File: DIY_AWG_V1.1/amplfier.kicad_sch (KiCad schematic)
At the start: 22 parts, among them IC3 LMH6505MAX, IC4 THS3091DDAR

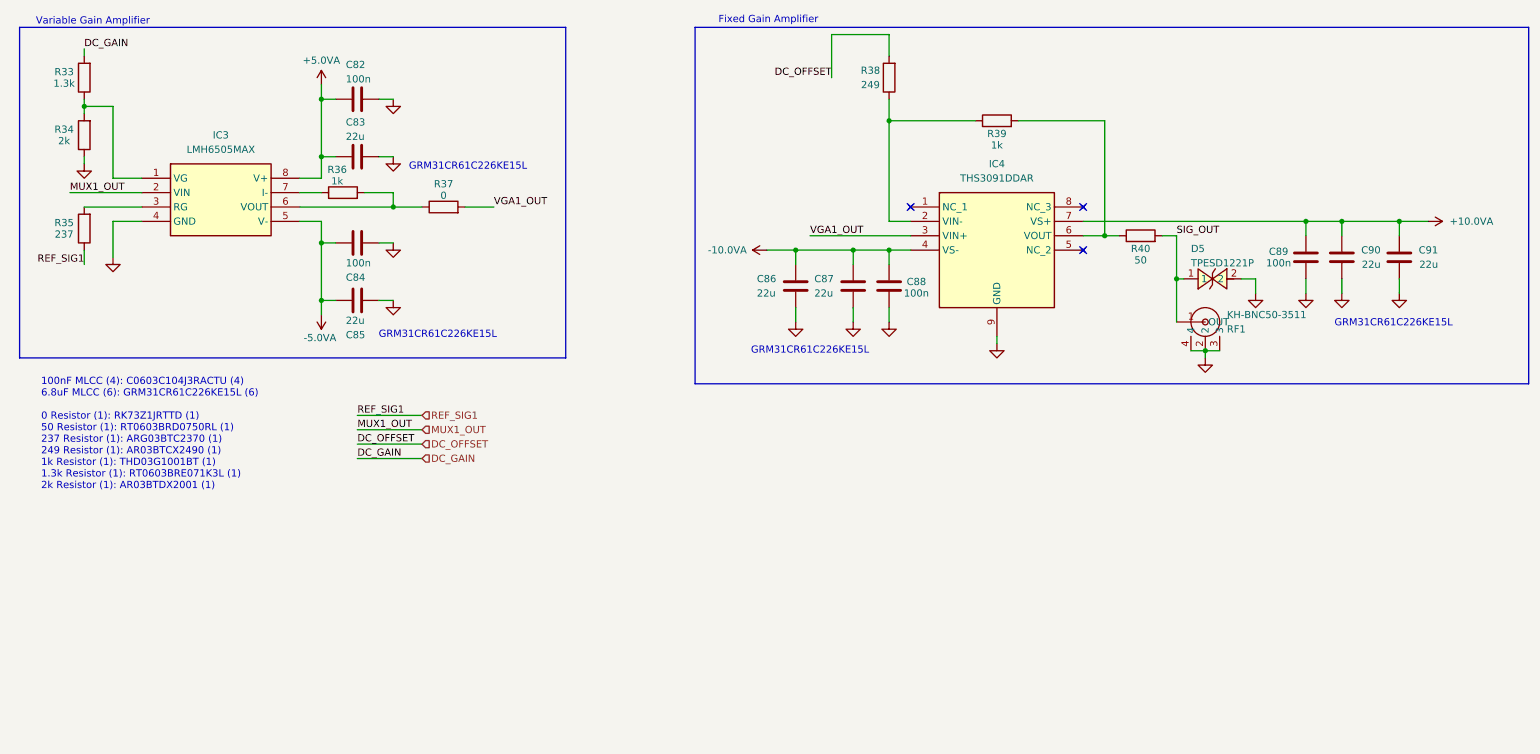
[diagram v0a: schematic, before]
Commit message: Updated to fix all ERCs
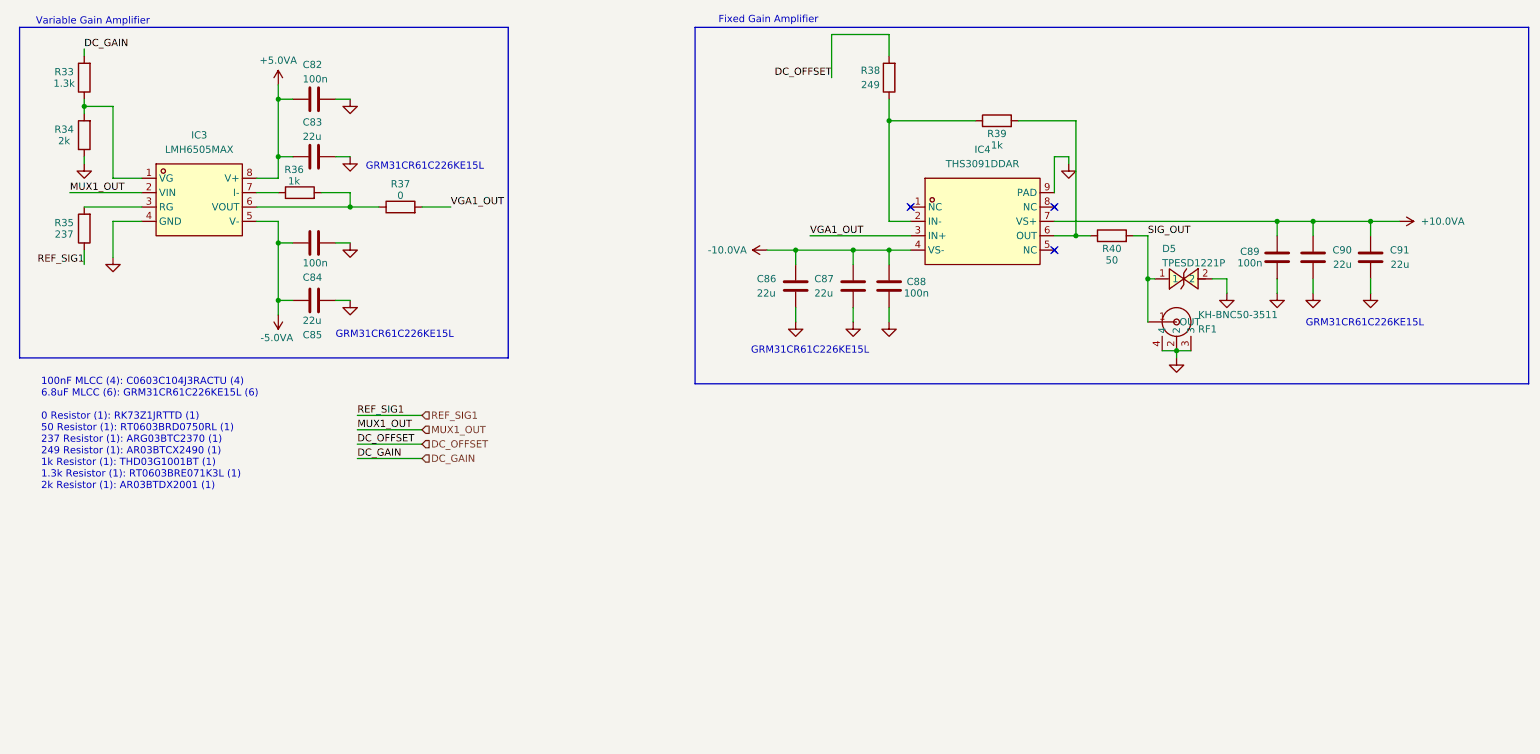
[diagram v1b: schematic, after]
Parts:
- removed IC3: LMH6505MAX, easyeda2kicad:SOP-8_L4.9-W3.9-P1.27-LS6.0-BL, symbol LMH6505MAX:LMH6505MAX
- removed IC4: THS3091DDAR, easyeda2kicad:SOIC-8_L4.9-W3.9-P1.27-LS6.0-BL-EP, symbol THS3091DDAR:THS3091DDAR
- added IC3: LMH6505MAX, easyeda2kicad:SOP-8_L4.9-W3.9-P1.27-LS6.0-BL, symbol easyeda2kicad:LMH6505MAX_NOPB
- added IC4: THS3091DDAR, easyeda2kicad:SOIC-8_L4.9-W3.9-P1.27-LS6.0-BL-EP, symbol easyeda2kicad:THS3091DDAR
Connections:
- net +10.0VA: now also IC4.7 (VS+)
- net +5.0VA: now also IC3.8 (V+)
- net -10.0VA: now also IC4.4 (VS-)
- net -5.0VA: now also IC3.5 (V-)
- net GND: now also IC3.4 (GND), IC4.9 (PAD)
- net MUX1_OUT: now also IC3.2 (VIN)
- net VGA1_OUT: now also IC4.3 (IN+)
- net at R39.2, R40.1: now also IC4.6 (OUT)
- net at R33.1, R34.2: now also IC3.1 (VG)
- net at R35.2: now also IC3.3 (RG)
- net at R36.2, R37.1: now also IC3.6 (VOUT)
- net at R36.1: now also IC3.7 (I-)
- net at R38.1, R39.1: now also IC4.2 (IN-)
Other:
- moved on the sheet: C82, C83, C84, C85, C89, C90, C91, D5, R36, R37, R40, RF1

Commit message: Updated component footprints
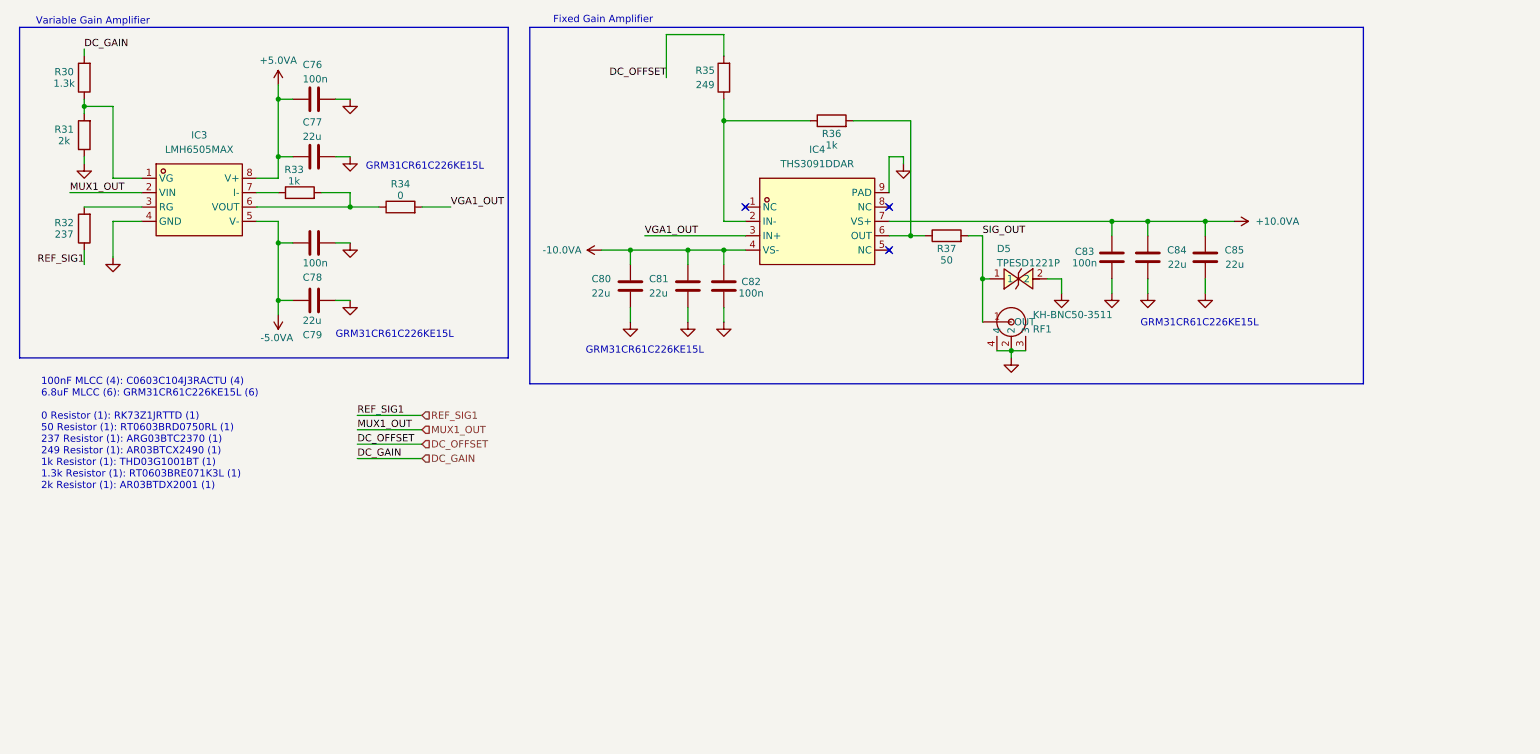
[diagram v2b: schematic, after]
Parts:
- renumbered C82 to C76, C83 to C77, C84 to C78, C85 to C79, C86 to C80, C87 to C81, C88 to C82, C89 to C83, C90 to C84, C91 to C85, R33 to R30, R34 to R31, R35 to R32, R36 to R33, R37 to R34, R38 to R35, R39 to R36, R40 to R37
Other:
- moved on the sheet: C80, C81, C82, C83, C84, C85, D5, IC4, R35, R36, R37, RF1

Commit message: Updated schematic footprints
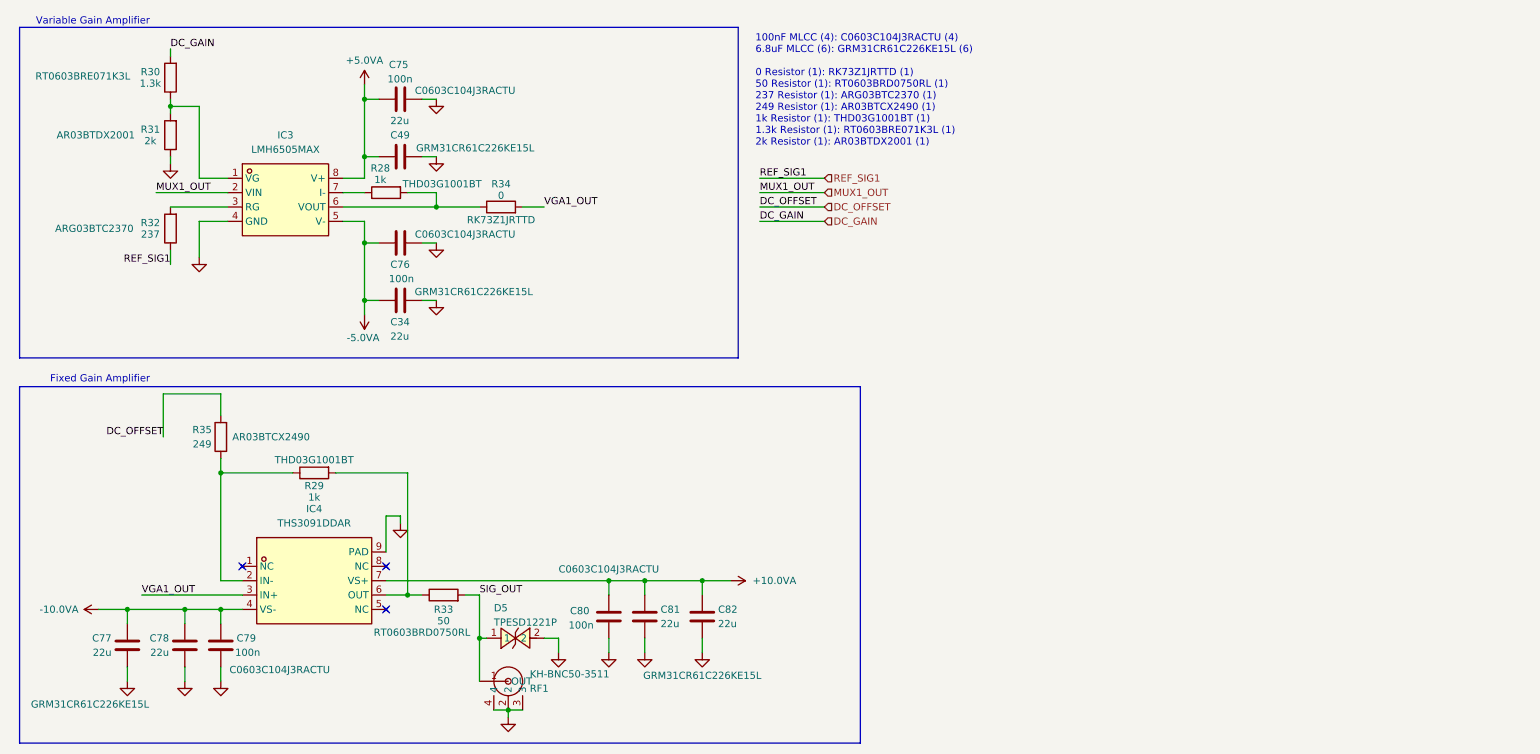
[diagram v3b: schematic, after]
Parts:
- removed C83: 100n, symbol Device:C
- removed C84, C85: 22u, symbol Device:C
- removed R36: 1k, symbol Device:R
- removed R37: 50, symbol Device:R
- added C34, C49: 22u, Capacitor_SMD:C_1206_3216Metric, symbol Device:C
- added C75: 100n, Capacitor_SMD:C_0603_1608Metric, symbol Device:C
- added R28, R29: 1k, Resistor_SMD:R_0603_1608Metric, symbol Device:R
- C76: footprint (none) -> Capacitor_SMD:C_0603_1608Metric; Component Name (none) -> C0603C104J3RACTU; LCSC ID (none) -> C2167388
- C77, C81: footprint (none) -> Capacitor_SMD:C_1206_3216Metric; Component Name (none) -> GRM31CR61C226KE15L; LCSC ID (none) -> C77088
- C78, C82: value 100n -> 22u; footprint (none) -> Capacitor_SMD:C_1206_3216Metric; Component Name (none) -> GRM31CR61C226KE15L; LCSC ID (none) -> C77088
- C79, C80: value 22u -> 100n; footprint (none) -> Capacitor_SMD:C_0603_1608Metric; Component Name (none) -> C0603C104J3RACTU; LCSC ID (none) -> C2167388
- R30: footprint (none) -> Resistor_SMD:R_0603_1608Metric; Component Name (none) -> RT0603BRE071K3L; LCSC ID (none) -> C136957
- R31: footprint (none) -> Resistor_SMD:R_0603_1608Metric; Component Name (none) -> AR03BTDX2001; LCSC ID (none) -> C319701
- R32: footprint (none) -> Resistor_SMD:R_0603_1608Metric; Component Name (none) -> ARG03BTC2370; LCSC ID (none) -> C2681612
- R33: value 1k -> 50; footprint (none) -> Resistor_SMD:R_0603_1608Metric; Component Name (none) -> RT0603BRD0750RL; LCSC ID (none) -> C5879483
- R34: footprint (none) -> Resistor_SMD:R_0603_1608Metric; Component Name (none) -> RK73Z1JRTTD; LCSC ID (none) -> C2596815
- R35: footprint (none) -> Resistor_SMD:R_0603_1608Metric; Component Name (none) -> AR03BTCX2490; LCSC ID (none) -> C2984337
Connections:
- net +10.0VA: now also C80.1, C81.1, C82.1
- net +5.0VA: now also C49.2, C75.2; no longer C76.1, C77.1
- net -10.0VA: now also C77.1, C78.1, C79.1; no longer C80.2, C81.2, C82.2
- net -5.0VA: now also C76.2, C34.2; no longer C78.1, C79.1
- net GND: now also C76.1, C80.2, C81.2, C82.2, C34.1, C49.1, C75.1; no longer C76.2, C80.1, C81.1, C82.1
- net SIG_OUT: now also R33.2
- net at IC4.6 (OUT): now also R33.1, R29.2
- net at IC4.2 (IN-), R35.1: now also R29.1
- net at IC3.6 (VOUT), R34.1: now also R28.2; no longer R33.2
- net at IC3.7 (I-): now also R28.1; no longer R33.1
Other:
- note removed: "GRM31CR61C226KE15L"
- moved on the sheet: D5, IC3, IC4, R30, R31, R32, R34, R35, RF1

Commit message: Updated schematics
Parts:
- removed R34: 0, Resistor_SMD:R_0603_1608Metric, symbol Device:R
- added R41: 0, Resistor_SMD:R_0603_1608Metric, symbol Device:R
- added RF11: IPEX-01, easyeda2kicad:IPEX-SMD_3P-L2.6-W2.6-LS3.0_YUANDI_RF-001, symbol easyeda2kicad:IPEX-01
- renumbered C77 to C76, C78 to C77, C79 to C78, C75 to C79, C49 to C80, C76 to C81, C34 to C82, C80 to C83, C81 to C84, C82 to C85, R30 to R34, R31 to R35, R32 to R36, R35 to R37, R29 to R38, R28 to R39, R33 to R40, RF1 to RF10
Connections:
- net GND: now also RF11.2, RF11.3
- net VGA1_OUT: now also IC3.6 (VOUT), R39.2, R41.2
- new net: R41.1, RF11.1

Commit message: Edited the electrical schematics, PCB design
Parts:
- removed RF11: IPEX-01, easyeda2kicad:IPEX-SMD_3P-L2.6-W2.6-LS3.0_YUANDI_RF-001, symbol easyeda2kicad:IPEX-01
- added CN10: RH-5019, easyeda2kicad:TESTPOINT-SMD_L3.8-W2.0_RH-5019, symbol easyeda2kicad:RH-5019
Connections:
- net at R41.1: now also CN10.1
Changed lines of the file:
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@@
 	(wire
 		(pts
-			(xy 109.22 68.58) (xy 111.76 68.58)
-		)
-		(stroke
-			(width 0)
-			(type default)
-		)
-	)
-	(wire
-		(pts
 			(xy 83.82 45.72) (xy 88.9 45.72)
 		)
@@
 	(wire
 		(pts
-			(xy 109.22 71.12) (xy 109.22 68.58)
-		)
-		(stroke
-			(width 0)
-			(type default)
-		)
-	)
-	(wire
-		(pts
 			(xy 80.01 102.87) (xy 82.55 102.87)
 		)
@@
 	(wire
 		(pts
-			(xy 127 68.58) (xy 129.54 68.58)
-		)
-		(stroke
-			(width 0)
-			(type default)
-		)
-	)
-	(wire
-		(pts
 			(xy 83.82 116.84) (xy 86.36 116.84)
 		)
@@
 	(wire
 		(pts
-			(xy 129.54 71.12) (xy 129.54 68.58)
-		)
-		(stroke
-			(width 0)
-			(type default)
-		)
-	)
-	(wire
-		(pts
 			(xy 80.01 114.3) (xy 119.38 114.3)
 		)
@@
 	(symbol
 		(lib_id "power:GND")
-		(at 109.22 71.12 0)
-		(mirror y)
-		(unit 1)
-		(body_style 1)
-		(exclude_from_sim no)
-		(in_bom yes)
-		(on_board yes)
-		(in_pos_files yes)
-		(dnp no)
-		(fields_autoplaced yes)
-		(property "Reference" "#PWR0199"
-			(at 109.22 77.47 0)
-			(hide yes)
-			(show_name no)
-			(do_not_autoplace no)
-			(effects
-				(font
-					(size 1.27 1.27)
-				)
-			)
-		)
-		(property "Value" "GND"
-			(at 109.22 76.2 0)
-			(hide yes)
-			(show_name no)
-			(do_not_autoplace no)
-			(effects
-				(font
-					(size 1.27 1.27)
-				)
-			)
-		)
-		(property "Footprint" ""
-			(at 109.22 71.12 0)
-			(hide yes)
-			(show_name no)
-			(do_not_autoplace no)
-			(effects
-				(font
-					(size 1.27 1.27)
-				)
-			)
-		)
-		(property "Datasheet" ""
-			(at 109.22 71.12 0)
-			(hide yes)
-			(show_name no)
-			(do_not_autoplace no)
-			(effects
-				(font
-					(size 1.27 1.27)
-				)
-			)
-		)
-		(property "Description" "Power symbol creates a global label with name \"GND\" , ground"
-			(at 109.22 71.12 0)
-			(hide yes)
-			(show_name no)
-			(do_not_autoplace no)
-			(effects
-				(font
-					(size 1.27 1.27)
-				)
-			)
-		)
-		(pin "1"
-		)
-		(instances
-			(project "DIY_AWG_V1.1"
-				(path "/508078af-d961-4af3-840e-a064a9f8d5bc/faa0e7f2-4ad4-4392-8346-980541b6a840"
-					(reference "#PWR0199")
-					(unit 1)
-				)
-			)
-		)
-	)
-	(symbol
-		(lib_id "power:GND")
 		(at 34.29 132.08 0)
 		(unit 1)
@@
 	)
 	(symbol
-		(lib_id "power:GND")
-		(at 129.54 71.12 0)
-		(mirror y)
-		(unit 1)
-		(body_style 1)
-		(exclude_from_sim no)
-		(in_bom yes)
-		(on_board yes)
-		(in_pos_files yes)
-		(dnp no)
-		(fields_autoplaced yes)
-		(property "Reference" "#PWR0203"
-			(at 129.54 77.47 0)
-			(hide yes)
-			(show_name no)
-			(do_not_autoplace no)
-			(effects
-				(font
-					(size 1.27 1.27)
-				)
-			)
-		)
-		(property "Value" "GND"
-			(at 129.54 76.2 0)
-			(hide yes)
-			(show_name no)
-			(do_not_autoplace no)
-			(effects
-				(font
-					(size 1.27 1.27)
-				)
-			)
-		)
-		(property "Footprint" ""
-			(at 129.54 71.12 0)
-			(hide yes)
-			(show_name no)
-			(do_not_autoplace no)
-			(effects
-				(font
-					(size 1.27 1.27)
-				)
-			)
-		)
-		(property "Datasheet" ""
-			(at 129.54 71.12 0)
-			(hide yes)
-			(show_name no)
-			(do_not_autoplace no)
-			(effects
-				(font
-					(size 1.27 1.27)
-				)
-			)
-		)
-		(property "Description" "Power symbol creates a global label with name \"GND\" , ground"
-			(at 129.54 71.12 0)
-			(hide yes)
-			(show_name no)
-			(do_not_autoplace no)
-			(effects
-				(font
-					(size 1.27 1.27)
-				)
-			)
-		)
-		(pin "1"
-		)
-		(instances
-			(project "DIY_AWG_V1.1"
-				(path "/508078af-d961-4af3-840e-a064a9f8d5bc/faa0e7f2-4ad4-4392-8346-980541b6a840"
-					(reference "#PWR0203")
-					(unit 1)
-				)
-			)
-		)
-	)
-	(symbol
 		(lib_id "Device:C")
 		(at 34.29 125.73 0)
@@
 	)
 	(symbol
+		(lib_id "easyeda2kicad:RH-5019")
+		(at 119.38 64.77 270)
+		(unit 1)
+		(body_style 1)
+		(exclude_from_sim no)
+		(in_bom yes)
+		(on_board yes)
+		(in_pos_files yes)
+		(dnp no)
+		(fields_autoplaced yes)
+		(property "Reference" "CN10"
+			(at 123.19 64.7699 90)
+			(show_name no)
+			(do_not_autoplace no)
+			(effects
+				(font
+					(size 1.27 1.27)
+				)
+				(justify left)
+			)
+		)
+		(property "Value" "RH-5019"
+			(at 123.19 67.3099 90)
+			(show_name no)
+			(do_not_autoplace no)
+			(effects
+				(font
+					(size 1.27 1.27)
+				)
+				(justify left)
+			)
+		)
+		(property "Footprint" "easyeda2kicad:TESTPOINT-SMD_L3.8-W2.0_RH-5019"
+			(at 111.76 64.77 0)
+			(hide yes)
+			(show_name no)
+			(do_not_autoplace no)
+			(effects
+				(font
+					(size 1.27 1.27)
+				)
+			)
+		)
+		(property "Datasheet" "https://www.lcsc.com/datasheet/C5199800.pdf"
+			(at 109.22 64.77 0)
+			(hide yes)
+			(show_name no)
+			(do_not_autoplace no)
+			(effects
+				(font
+					(size 1.27 1.27)
+				)
+			)
+		)
+		(property "Description" ""
+			(at 119.38 64.77 0)
+			(hide yes)
+			(show_name no)
+			(do_not_autoplace no)
+			(effects
+				(font
+					(size 1.27 1.27)
+				)
+			)
+		)
+		(property "Manufacturer" "荣和"
+			(at 106.68 64.77 0)
+			(hide yes)
+			(show_name no)
+			(do_not_autoplace no)
+			(effects
+				(font
+					(size 1.27 1.27)
+				)
+			)
+		)
+		(property "MPN" "RH-5019"
+			(at 104.14 64.77 0)
+			(hide yes)
+			(show_name no)
+			(do_not_autoplace no)
+			(effects
+				(font
+					(size 1.27 1.27)
+				)
+			)
+		)
+		(property "LCSC Part" "C5199800"
+			(at 101.6 64.77 0)
+			(hide yes)
+			(show_name no)
+			(do_not_autoplace no)
+			(effects
+				(font
+					(size 1.27 1.27)
+				)
+			)
+		)
+		(pin "1"
+		)
+		(instances
+			(project "DIY_AWG_V1.1"
+				(path "/508078af-d961-4af3-840e-a064a9f8d5bc/faa0e7f2-4ad4-4392-8346-980541b6a840"
+					(reference "CN10")
+					(unit 1)
+				)
+			)
+		)
+	)
+	(symbol
 		(lib_id "power:GND")
 		(at 50.8 132.08 0)
@@
 					(unit 1)
 				)
-			)
-		)
-	)
-	(symbol
-		(lib_id "easyeda2kicad:IPEX-01")
-		(at 119.38 66.04 0)
-		(unit 1)
-		(body_style 1)
-		(exclude_from_sim no)
-		(in_bom yes)
-		(on_board yes)
-		(in_pos_files yes)
-		(dnp no)
-		(property "Reference" "RF11"
-			(at 127 62.23 0)
-			(show_name no)
-			(do_not_autoplace no)
-			(effects
-				(font
-					(size 1.27 1.27)
-				)
-			)
-		)
-		(property "Value" "IPEX-01"
-			(at 127 64.77 0)
-			(show_name no)
-			(do_not_autoplace no)
-			(effects
-				(font
-					(size 1.27 1.27)
-				)
-			)
-		)
-		(property "Footprint" "easyeda2kicad:IPEX-SMD_3P-L2.6-W2.6-LS3.0_YUANDI_RF-001"
-			(at 119.38 76.2 0)
-			(hide yes)
-			(show_name no)
-			(do_not_autoplace no)
-			(effects
-				(font
-					(size 1.27 1.27)
-				)
-			)
-		)
-		(property "Datasheet" "https://www.lcsc.com/datasheet/C36936657.pdf"
-			(at 119.38 78.74 0)
-			(hide yes)
-			(show_name no)
-			(do_not_autoplace no)
-			(effects
-				(font
-					(size 1.27 1.27)
-				)
-			)
-		)
-		(property "Description" ""
-			(at 119.38 66.04 0)
-			(hide yes)
-			(show_name no)
-			(do_not_autoplace no)
-			(effects
-				(font
-					(size 1.27 1.27)
-				)
-			)
-		)
-		(property "Manufacturer" "BXCONN(宝讯)"
-			(at 119.38 81.28 0)
-			(hide yes)
-			(show_name no)
-			(do_not_autoplace no)
-			(effects
-				(font
-					(size 1.27 1.27)
-				)
-			)
-		)
-		(property "MPN" "IPEX-01"
-			(at 119.38 83.82 0)
-			(hide yes)
-			(show_name no)
-			(do_not_autoplace no)
-			(effects
-				(font
-					(size 1.27 1.27)
-				)
-			)
-		)
-		(property "LCSC Part" "C36936657"
-			(at 119.38 86.36 0)
-			(hide yes)
-			(show_name no)
-			(do_not_autoplace no)
-			(effects
-				(font
-					(size 1.27 1.27)
-				)
-			)
-		)
-		(pin "2"
-		)
-		(pin "1"
-		)
-		(pin "3"
-		)
-		(instances
-			(project "DIY_AWG_V1.1"
-				(path "/508078af-d961-4af3-840e-a064a9f8d5bc/faa0e7f2-4ad4-4392-8346-980541b6a840"
-					(reference "RF11")
-					(unit 1)
-				)
